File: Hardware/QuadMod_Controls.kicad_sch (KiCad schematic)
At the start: 24 parts, among them J1 Conn_01x08_Pin, J10 Audio_Out_L, J11 Audio_Out_R, J2 Conn_01x08_Pin, J3 Conn_01x08_Pin, J4 Conn_01x08_Pin, J5 AudioJack2_Ground_Switch, J6 AudioJack2_Ground_Switch, J7 AudioJack2_Ground_Switch, J7 Audio_In, J8 AudioJack2_Ground_Switch, J9 AudioJack2_Ground_Switch, SW1 FX_Type_Switch

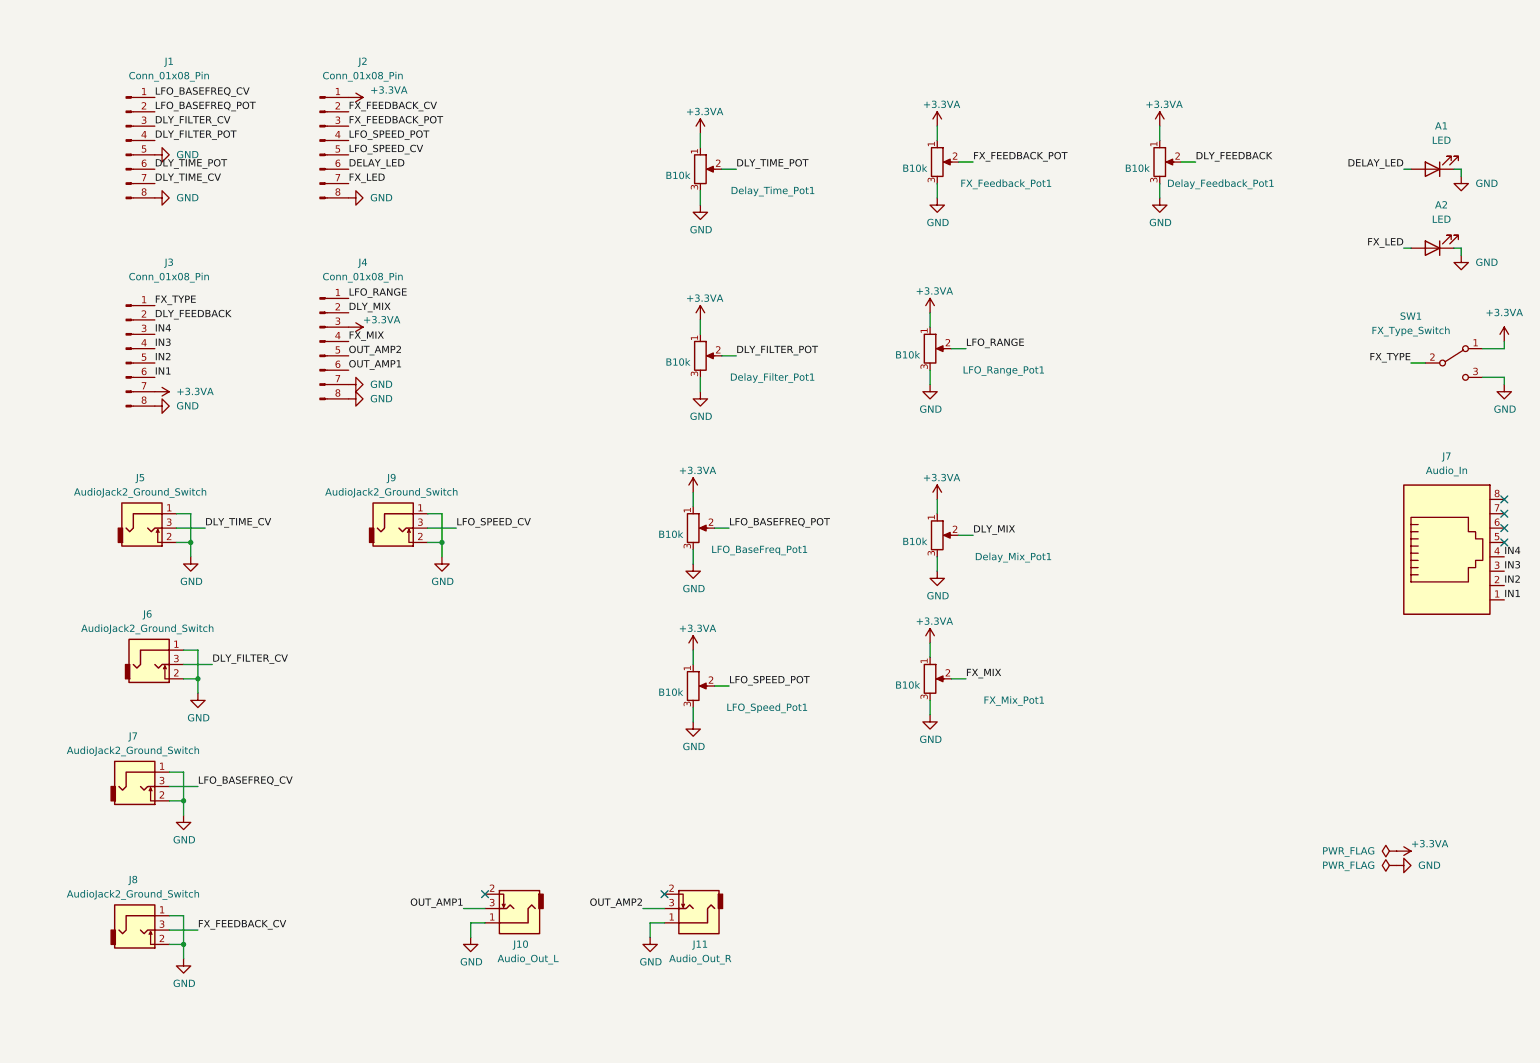
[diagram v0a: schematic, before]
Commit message: Started adding additional clock LED
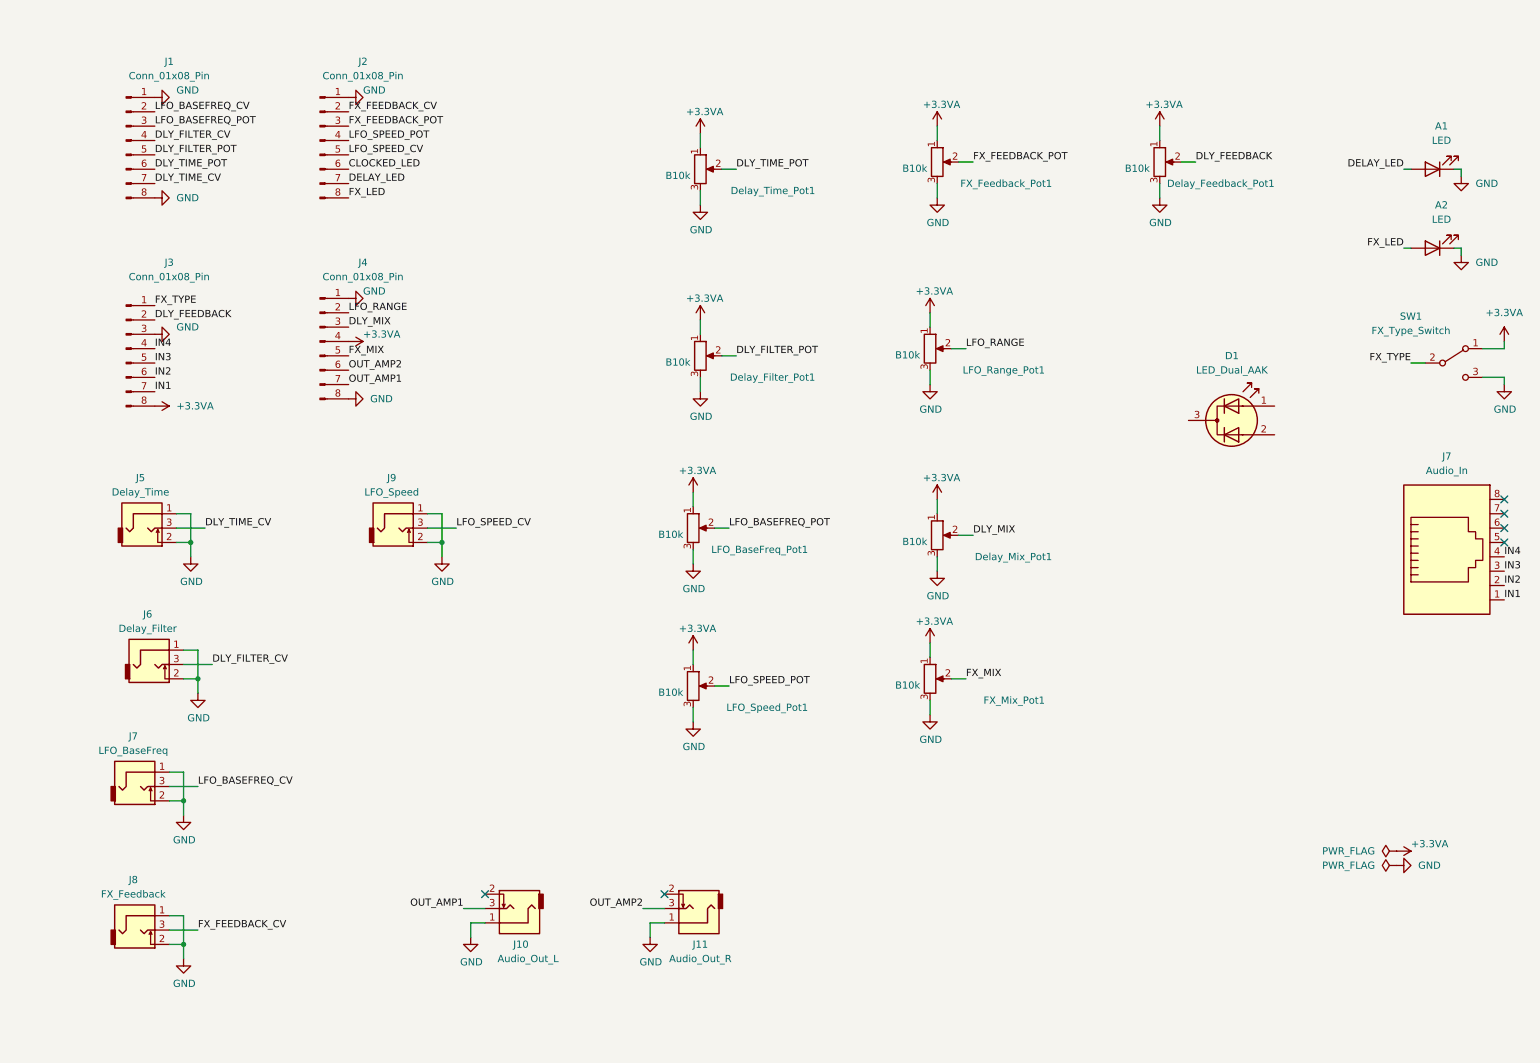
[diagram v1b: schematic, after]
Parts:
- added D1: LED_Dual_AAK, symbol Device:LED_Dual_AAK
- J5: value AudioJack2_Ground_Switch -> Delay_Time
- J6: value AudioJack2_Ground_Switch -> Delay_Filter
- J7: value AudioJack2_Ground_Switch -> LFO_BaseFreq
- J8: value AudioJack2_Ground_Switch -> FX_Feedback
- J9: value AudioJack2_Ground_Switch -> LFO_Speed
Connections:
- net +3.3VA: now also J3.8 (Pin_8), J4.4 (Pin_4); no longer J2.1 (Pin_1), J3.7 (Pin_7), J4.3 (Pin_3)
- net DELAY_LED: now also J2.7 (Pin_7); no longer J2.6 (Pin_6)
- net DLY_FILTER_CV: now also J1.4 (Pin_4); no longer J1.3 (Pin_3)
- net DLY_FILTER_POT: now also J1.5 (Pin_5); no longer J1.4 (Pin_4)
- net DLY_MIX: now also J4.3 (Pin_3); no longer J4.2 (Pin_2)
- net FX_LED: now also J2.8 (Pin_8); no longer J2.7 (Pin_7)
- net FX_MIX: now also J4.5 (Pin_5); no longer J4.4 (Pin_4)
- net GND: now also J1.1 (Pin_1), J2.1 (Pin_1), J3.3 (Pin_3), J4.1 (Pin_1); no longer J1.5 (Pin_5), J2.8 (Pin_8), J3.8 (Pin_8), J4.7 (Pin_7)
- net IN1: now also J3.7 (Pin_7); no longer J3.6 (Pin_6)
- net IN2: now also J3.6 (Pin_6); no longer J3.5 (Pin_5)
- net IN3: now also J3.5 (Pin_5); no longer J3.4 (Pin_4)
- net IN4: now also J3.4 (Pin_4); no longer J3.3 (Pin_3)
- net LFO_BASEFREQ_CV: now also J1.2 (Pin_2); no longer J1.1 (Pin_1)
- net LFO_BASEFREQ_POT: now also J1.3 (Pin_3); no longer J1.2 (Pin_2)
- net LFO_RANGE: now also J4.2 (Pin_2); no longer J4.1 (Pin_1)
- net OUT_AMP1: now also J4.7 (Pin_7); no longer J4.6 (Pin_6)
- net OUT_AMP2: now also J4.6 (Pin_6); no longer J4.5 (Pin_5)
- new net CLOCKED_LED: J2.6 (Pin_6)

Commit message: Clean up of schematics and PCBS
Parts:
- removed A1: LED, Custom_Footprints:LED_D3.0mm, symbol Device:LED
- Delay_LED1: renamed from D1; value LED_Dual_AAK -> LED_Dual_AKA; footprint (none) -> Custom_Footprints:LED_D3.0mm-3; symbol Device:LED_Dual_AAK -> Device:LED_Dual_AKA
- SW1: footprint Custom_Footprints:SPDTSubMiniature -> Custom_Footprints:SPDT_Miniature
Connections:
- net CLOCKED_LED: now also Delay_LED1.1 (A1)
- net DELAY_LED: now also Delay_LED1.3 (A2)
- net GND: now also Delay_LED1.2 (K)
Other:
- note added: "Connectors"
- note added: "I/O Sockets"
- note added: "LEDs and Switches"
- note added: "Potentiometers"
- company: (none) -> Mountjoy Modular
- title: (none) -> QuadMod Controls
- moved on the sheet: A2, Delay_Feedback_Pot1, Delay_Filter_Pot1, Delay_LED1, Delay_Mix_Pot1, Delay_Time_Pot1, FX_Feedback_Pot1, FX_Mix_Pot1, J1, J10, J11, J2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

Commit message: Draft Gerber Creation
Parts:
- J1, J2, J3, J4: footprint Connector_PinHeader_2.54mm:PinHeader_1x08_P2.54mm_Vertical -> Connector_PinSocket_2.54mm:PinSocket_1x08_P2.54mm_Vertical
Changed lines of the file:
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@@
       (effects (font (size 1.27 1.27)))
     )
-    (property "Footprint" "Connector_PinHeader_2.54mm:PinHeader_1x08_P2.54mm_Vertical" (at 62.23 35.56 0)
+    (property "Footprint" "Connector_PinSocket_2.54mm:PinSocket_1x08_P2.54mm_Vertical" (at 62.23 35.56 0)
       (effects (font (size 1.27 1.27)) hide)
     )
@@
       (effects (font (size 1.27 1.27)))
     )
-    (property "Footprint" "Connector_PinHeader_2.54mm:PinHeader_1x08_P2.54mm_Vertical" (at 62.23 71.12 0)
+    (property "Footprint" "Connector_PinSocket_2.54mm:PinSocket_1x08_P2.54mm_Vertical" (at 62.23 71.12 0)
       (effects (font (size 1.27 1.27)) hide)
     )
@@
       (effects (font (size 1.27 1.27)))
     )
-    (property "Footprint" "Connector_PinHeader_2.54mm:PinHeader_1x08_P2.54mm_Vertical" (at 27.94 35.56 0)
+    (property "Footprint" "Connector_PinSocket_2.54mm:PinSocket_1x08_P2.54mm_Vertical" (at 27.94 35.56 0)
       (effects (font (size 1.27 1.27)) hide)
     )
@@
       (effects (font (size 1.27 1.27)))
     )
-    (property "Footprint" "Connector_PinHeader_2.54mm:PinHeader_1x08_P2.54mm_Vertical" (at 27.94 72.39 0)
-      (effects (font (size 1.27 1.27)) hide)
-    )
+    (property "Footprint" "Connector_PinSocket_2.54mm:PinSocket_1x08_P2.54mm_Vertical" (at 27.94 72.39 0)
+      (effects (font (size 1.27 1.27)) hide)
+    )

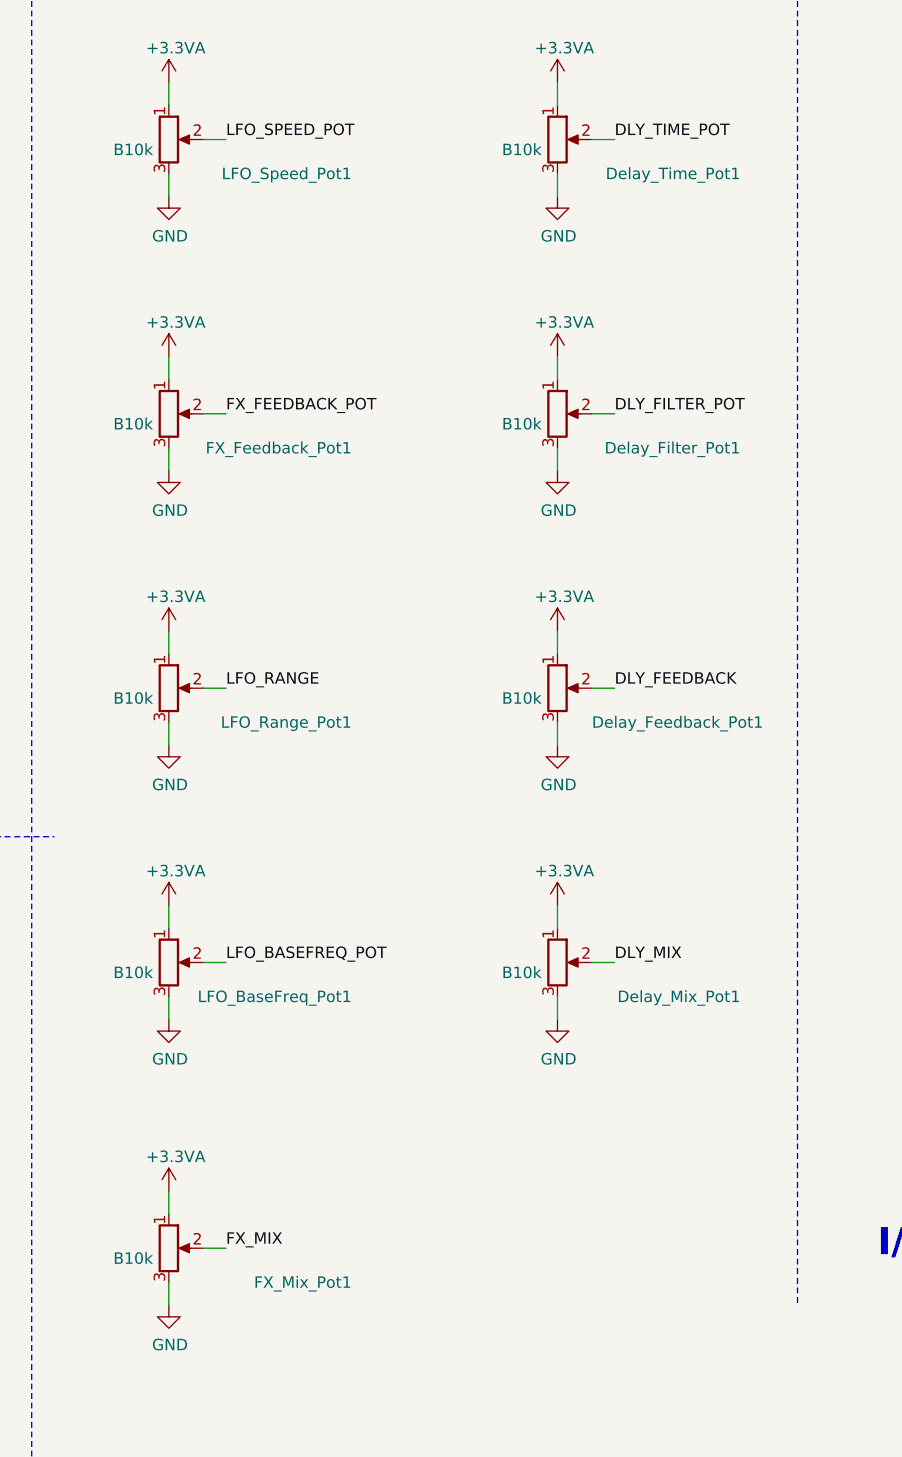
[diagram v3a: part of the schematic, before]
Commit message: Updated Production Gerbers; attempts to get USB working with O1 optimisation
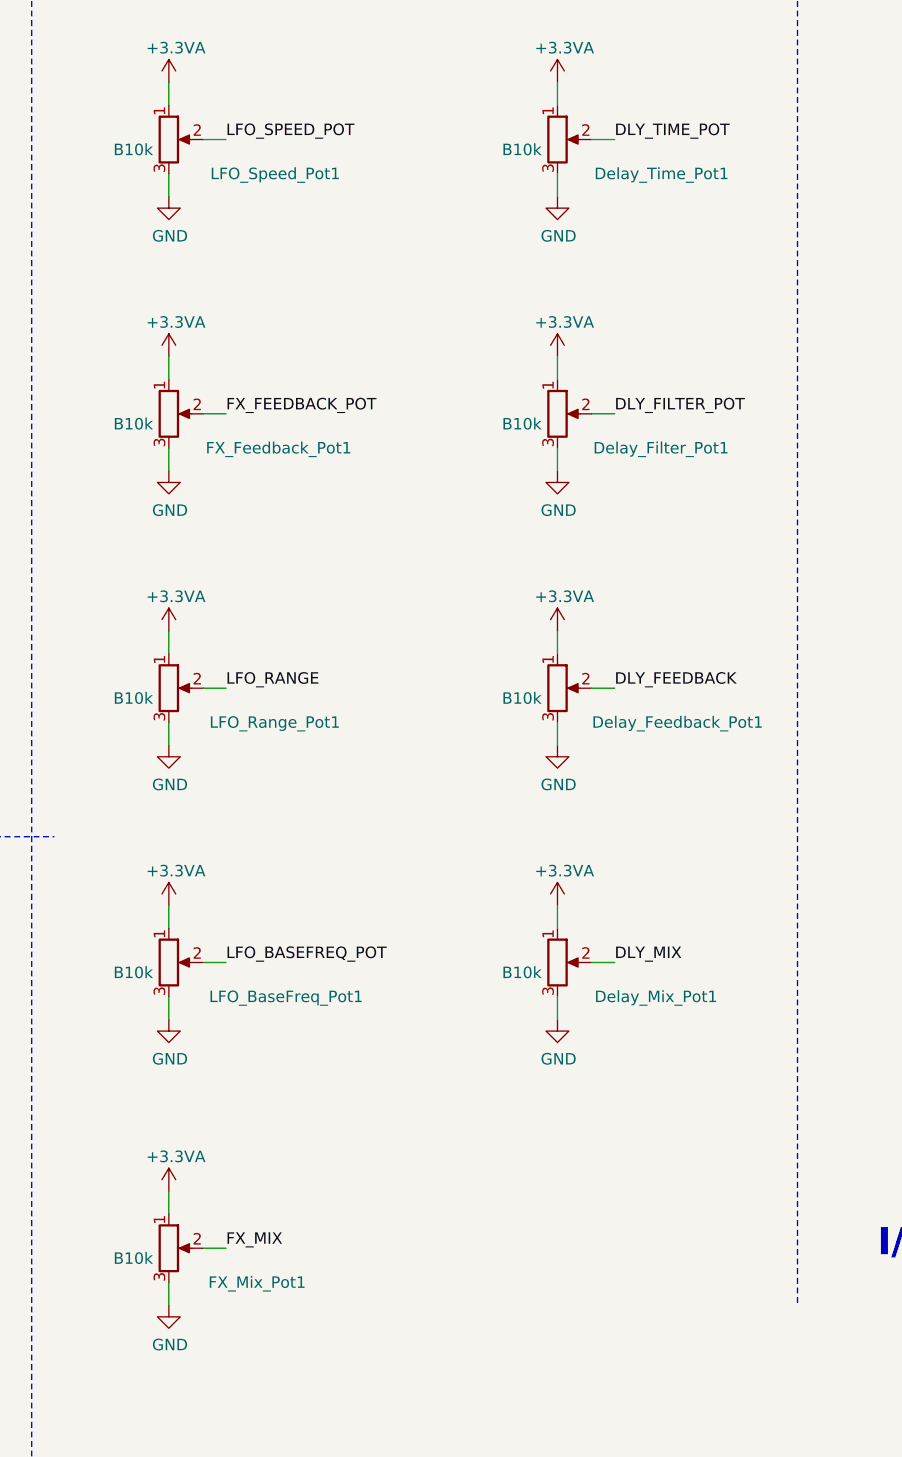
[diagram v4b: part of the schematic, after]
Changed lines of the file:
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@@
   (symbol (lib_id "Encoder:R_POT") (at 149.86 66.04 0) (unit 1)
     (in_bom yes) (on_board yes) (dnp no)
-    (property "Reference" "Delay_Filter_Pot1" (at 170.18 69.85 0)
+    (property "Reference" "Delay_Filter_Pot1" (at 168.91 69.85 0)
       (effects (font (size 1.27 1.27)) (justify right))
     )
@@
   (symbol (lib_id "Encoder:R_POT") (at 106.68 158.75 0) (unit 1)
     (in_bom yes) (on_board yes) (dnp no)
-    (property "Reference" "FX_Mix_Pot1" (at 127 162.56 0)
+    (property "Reference" "FX_Mix_Pot1" (at 121.92 162.56 0)
       (effects (font (size 1.27 1.27)) (justify right))
     )
@@
   (symbol (lib_id "Encoder:R_POT") (at 149.86 127 0) (unit 1)
     (in_bom yes) (on_board yes) (dnp no)
-    (property "Reference" "Delay_Mix_Pot1" (at 170.18 130.81 0)
+    (property "Reference" "Delay_Mix_Pot1" (at 167.64 130.81 0)
       (effects (font (size 1.27 1.27)) (justify right))
     )
@@
   (symbol (lib_id "Encoder:R_POT") (at 106.68 35.56 0) (unit 1)
     (in_bom yes) (on_board yes) (dnp no)
-    (property "Reference" "LFO_Speed_Pot1" (at 127 39.37 0)
+    (property "Reference" "LFO_Speed_Pot1" (at 125.73 39.37 0)
       (effects (font (size 1.27 1.27)) (justify right))
     )
@@
   (symbol (lib_id "Encoder:R_POT") (at 106.68 127 0) (unit 1)
     (in_bom yes) (on_board yes) (dnp no)
-    (property "Reference" "LFO_BaseFreq_Pot1" (at 127 130.81 0)
+    (property "Reference" "LFO_BaseFreq_Pot1" (at 128.27 130.81 0)
       (effects (font (size 1.27 1.27)) (justify right))
     )
@@
   (symbol (lib_id "Encoder:R_POT") (at 149.86 35.56 0) (unit 1)
     (in_bom yes) (on_board yes) (dnp no)
-    (property "Reference" "Delay_Time_Pot1" (at 170.18 39.37 0)
+    (property "Reference" "Delay_Time_Pot1" (at 168.91 39.37 0)
       (effects (font (size 1.27 1.27)) (justify right))
     )
@@
   (symbol (lib_id "Encoder:R_POT") (at 106.68 96.52 0) (unit 1)
     (in_bom yes) (on_board yes) (dnp no)
-    (property "Reference" "LFO_Range_Pot1" (at 127 100.33 0)
-      (effects (font (size 1.27 1.27)) (justify right))
-    )
+    (property "Reference" "LFO_Range_Pot1" (at 125.73 100.33 0)
+      (effects (font (size 1.27 1.27)) (justify right))
+    )
